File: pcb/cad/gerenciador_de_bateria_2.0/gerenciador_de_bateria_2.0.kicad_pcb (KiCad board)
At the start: 2 copper layers, 37 parts, among them J1 Conn_01x01_Female, J10 Conn_01x01_Female, J2 Conn_01x01_Female, J3 Conn_01x01_Female, J4 Conn_01x01_Female, J5 Conn_01x02_Male, J6 Conn_01x01_Female, J7 Conn_01x01_Female, J8 Conn_01x01_Female, J9 Conn_01x01_Female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

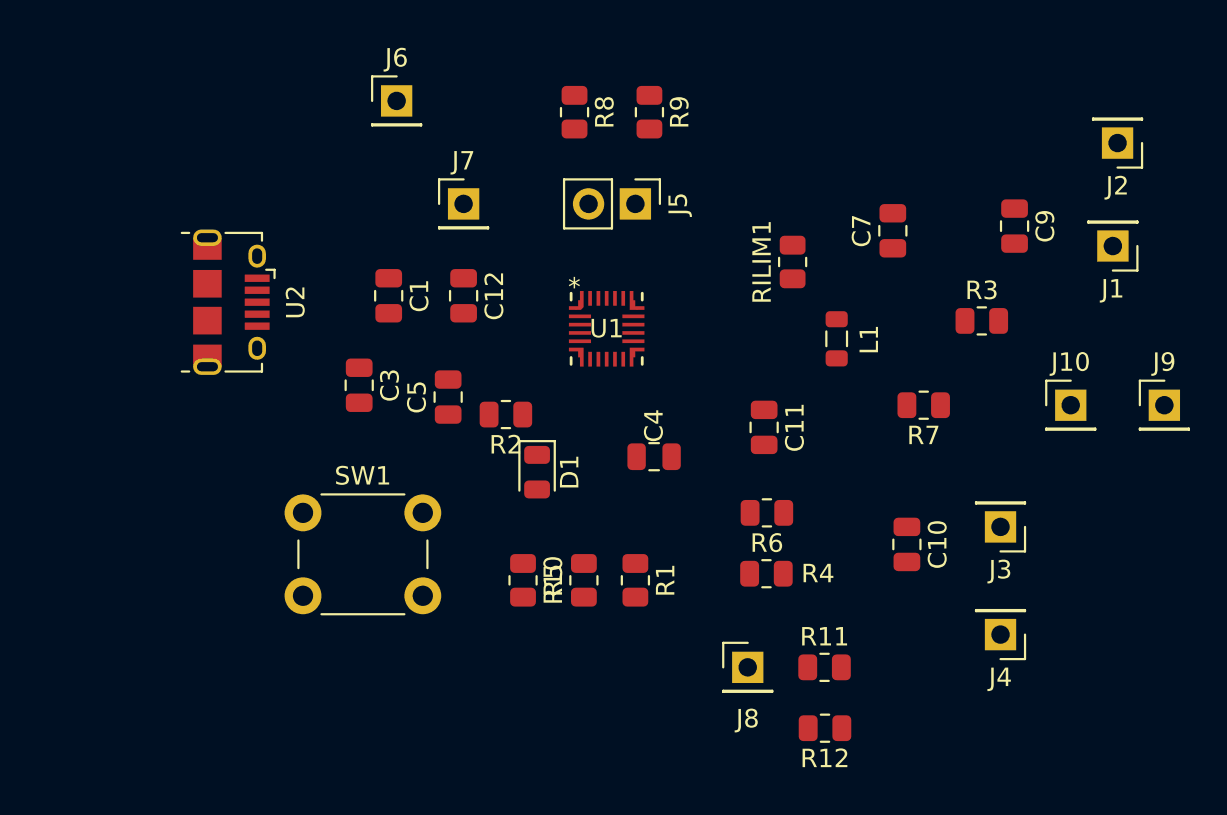
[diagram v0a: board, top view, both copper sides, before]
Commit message: Alteração no GND do esquemático para GNDA ou GNDPWR, finalização da PCB do gerenciador de bateria 2.0
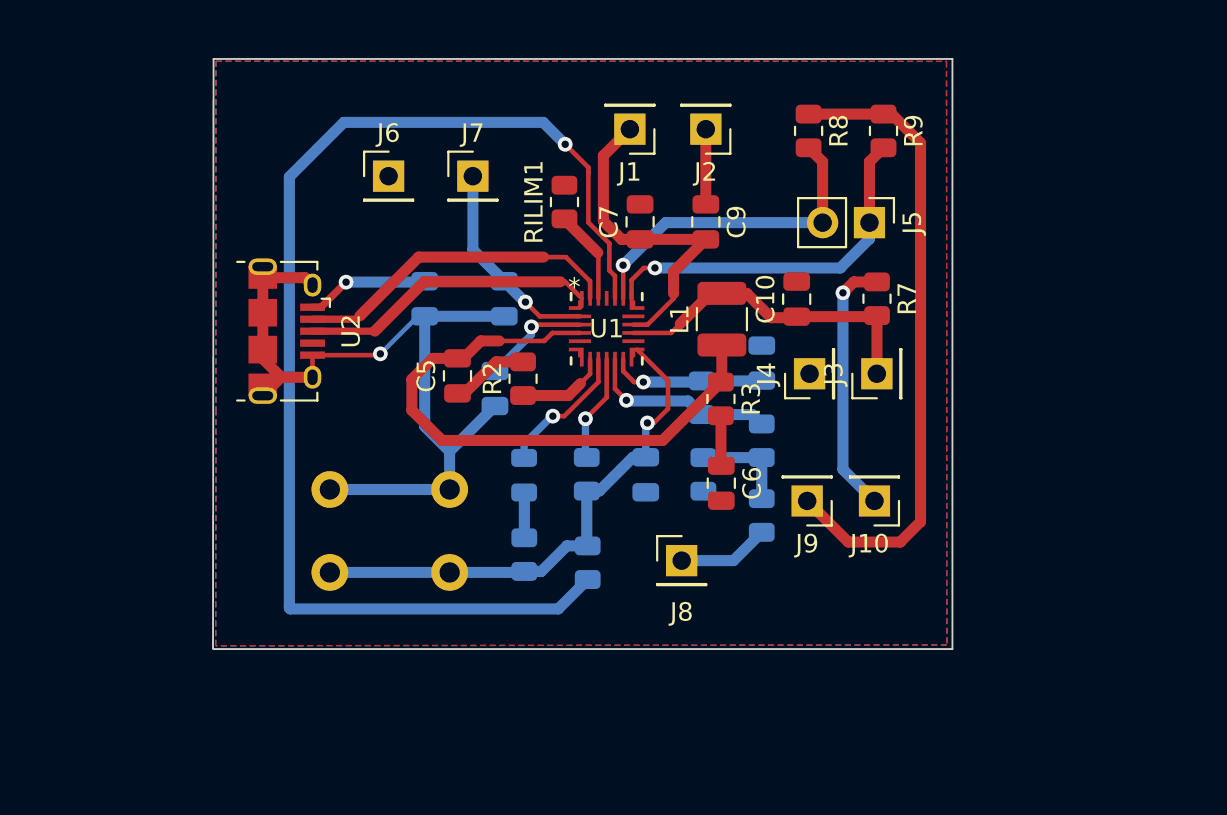
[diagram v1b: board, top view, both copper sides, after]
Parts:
- added C6: NC, Capacitor_SMD:C_0805_2012Metric, F.Cu at (125.8, 131.0)
- C1, C11, C12, C3, C4, D1, R1, R10, R11, R12, R4, R5, R6, SW1: moved to B.Cu
- L1: footprint Inductor_SMD:L_0805_2012Metric -> Inductor_SMD:L_1210_3225Metric
- moved J1 27.0 mm to (120.9, 111.8)
- moved J2 22.4 mm to (125.0, 111.8)
- moved J9 20.1 mm to (130.5, 131.9), turned to 180 degrees
- moved J4 17.5 mm to (130.6, 125.0), turned to 90 degrees
- moved C9 16.8 mm to (125.0, 116.8)
- moved R12 15.3 mm to (124.8, 130.5), turned to -90 degrees
- moved R3 14.8 mm to (125.8, 126.4), turned to -90 degrees
- moved C10 14.6 mm to (129.9, 121.0), turned to 90 degrees
- moved C7 13.7 mm to (121.4, 116.8)
- moved RILIM1 12.8 mm to (117.3, 115.7)
- moved R8 12.7 mm to (130.6, 111.9)
- moved J5 12.7 mm to (133.9, 116.8)
- moved R9 12.7 mm to (134.6, 111.9)
- moved J10 11.8 mm to (134.1, 131.9), turned to 180 degrees
- moved J3 10.7 mm to (134.3, 125.0), turned to 90 degrees
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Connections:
- C1 pad 2: GND -> GNDA
- C10 pad 2: GNDPWR -> GNDA
- C11 pad 1: GND -> GNDA
- C12 pad 2: GND -> GNDA
- C3 pad 2: GNDPWR -> GNDA
- C7 pad 2: GND -> GNDA
- C9 pad 1: GNDPWR -> GNDA
- J2 pad 1: GNDPWR -> GNDA
- J4 pad 1: GNDPWR -> GNDA
- J6 pad 1: GND -> GNDA
- RILIM1 pad 2: GND -> GNDA
- U1 pad 14: (no net) -> /VREF
- U1 pad 15: GND -> GNDA
- U1 pad 5: GND -> GNDA
- U1 pad 7: GND -> GNDA
- U2 pad 5: GND -> GNDA
- U2 pad 6: GND -> GNDA
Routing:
- net Net-(R1-Pad1): track 0.00 -> 66.4 mm, vias 0 -> 1
- net GNDA: track 0.00 -> 48.9 mm, vias 0 -> 1
- net /VDD: track 0.00 -> 34.8 mm
- net Net-(C5-Pad2): track 0.00 -> 32.6 mm
- net /VREF: track 0.00 -> 29.1 mm, vias 0 -> 1
- net Net-(C1-Pad1): track 0.00 -> 22.3 mm, vias 0 -> 2
- net /SCL: track 0.00 -> 20.1 mm, vias 0 -> 1
- net Net-(C7-Pad1): track 0.00 -> 18.7 mm
- net /SYS: track 0.00 -> 18.2 mm
- net /SDA: track 0.00 -> 18.0 mm, vias 0 -> 1
- net Net-(U2-Pad2): track 0.00 -> 17.9 mm
- net Net-(U2-Pad3): track 0.00 -> 16.1 mm
- net Net-(J10-Pad1): track 0.00 -> 14.1 mm, vias 0 -> 1
- net Net-(R4-Pad1): track 0.00 -> 10.4 mm, vias 0 -> 1
- net Net-(C11-Pad2): track 0.00 -> 8.44 mm, vias 0 -> 1
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- added copper zone on B.Cu, net GNDA
- added copper zone on F.Cu, net GNDA
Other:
- board outline added: 40.1 x 32 mm

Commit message: Otimização do esquemático do gerenciador_de_bateria, PCB atualizada com o USB centralizado no gerenciador_de_bateria_2.0, no gerenciador_de_bateria a PCB foi inicializada e finalizada
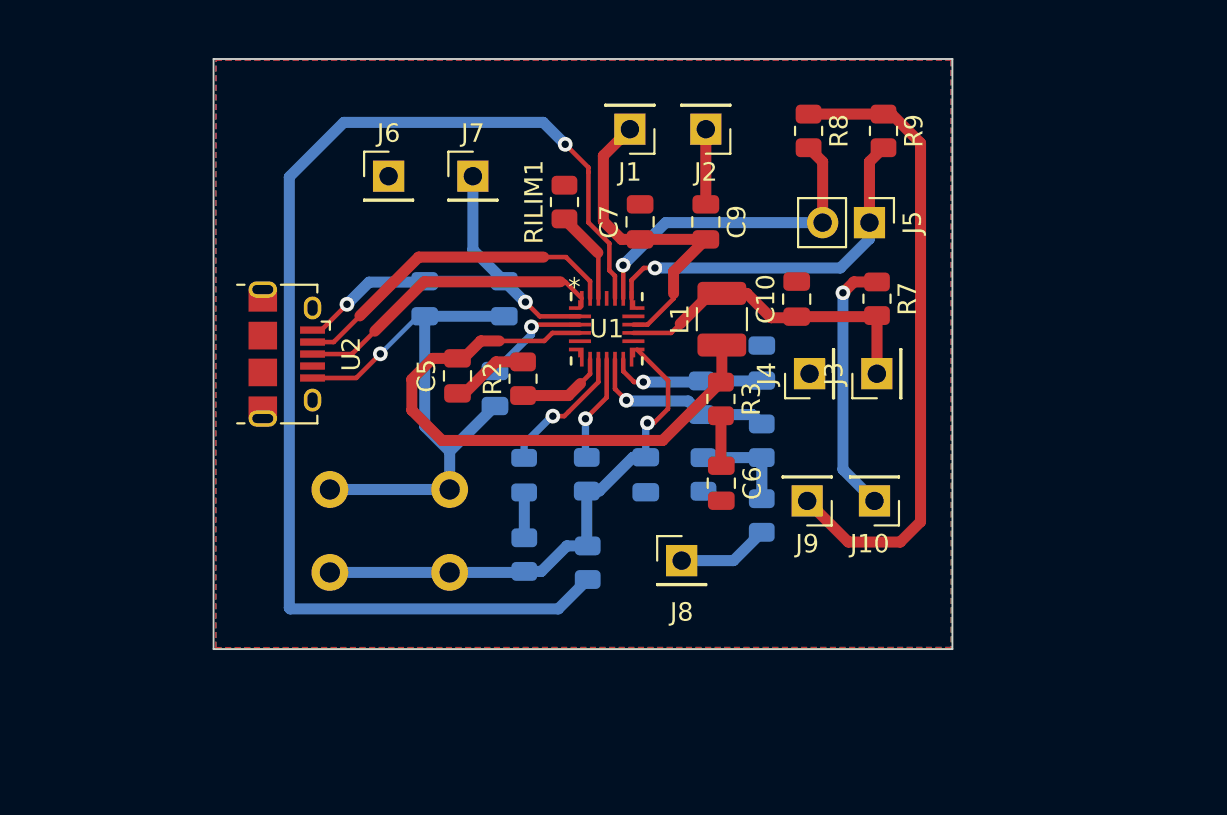
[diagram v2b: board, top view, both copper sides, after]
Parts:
- moved U2 1.24 mm to (102.2, 124.0)
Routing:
- net GNDA: track 48.9 -> 35.8 mm
- net Net-(C1-Pad1): track 22.3 -> 22.8 mm
- net Net-(U2-Pad3): track 16.1 -> 16.6 mm
- net Net-(U2-Pad2): track 17.9 -> 18.4 mm
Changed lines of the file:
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@@
   )
   (footprint "Connector_USB:USB_Micro-B_Amphenol_10118194_Horizontal" (layer "F.Cu")
-    (at 102.24 122.73 -90)
+    (at 102.24 123.97 -90)
     (descr "USB Micro-B receptacle, horizontal, SMD, 10118194, https://cdn.amphenol-icc.com/media/wysiwyg/files/drawing/10118194.pdf")
     (tags "USB Micro B horizontal SMD")
@@
     )
   )
-  (gr_line (start 98.25 139.98) (end 138.36 139.98) (layer "Edge.Cuts") (width 0.1))
+  (gr_line (start 98.27 139.98) (end 138.36 139.98) (layer "Edge.Cuts") (width 0.1))
   (gr_line (start 138.36 139.98) (end 138.36 107.96) (layer "Edge.Cuts") (width 0.1))
-  (gr_line (start 98.27 107.96) (end 98.24 139.93) (layer "Edge.Cuts") (width 0.1))
+  (gr_line (start 98.27 107.96) (end 98.27 139.98) (layer "Edge.Cuts") (width 0.1))
   (gr_line (start 138.36 107.96) (end 98.27 107.96) (layer "Edge.Cuts") (width 0.1))
-  (segment (start 104.1 121.43) (end 103.64 121.43) (width 0.4) (layer "F.Cu") (net 1))
   (segment (start 115.967735 121.925) (end 115.192816 121.150081) (width 0.25) (layer "F.Cu") (net 1))
-  (segment (start 105.46 120.07) (end 104.1 121.43) (width 0.4) (layer "F.Cu") (net 1))
+  (segment (start 103.64 122.67) (end 104.115 122.67) (width 0.25) (layer "F.Cu") (net 1))
+  (segment (start 104.115 122.67) (end 105.46 121.325) (width 0.25) (layer "F.Cu") (net 1))
+  (segment (start 105.46 121.325) (end 105.46 121.32) (width 0.25) (layer "F.Cu") (net 1))
+  (segment (start 105.46 121.32) (end 105.51 121.27) (width 0.25) (layer "F.Cu") (net 1))
   (segment (start 118.15 121.925) (end 115.967735 121.925) (width 0.25) (layer "F.Cu") (net 1))
   (via (at 115.192816 121.150081) (size 0.8) (drill 0.4) (layers "F.Cu" "B.Cu") (net 1))
-  (via (at 105.46 120.07) (size 0.8) (drill 0.4) (layers "F.Cu" "B.Cu") (net 1))
+  (via (at 105.51 121.27) (size 0.8) (drill 0.4) (layers "F.Cu" "B.Cu") (net 1))
   (segment (start 112.34 118.314) (end 114.046 120.02) (width 0.6) (layer "B.Cu") (net 1))
   (segment (start 114.046 120.026) (end 115.18 121.16) (width 0.6) (layer "B.Cu") (net 1))
+  (segment (start 106.71 120.07) (end 109.678 120.07) (width 0.6) (layer "B.Cu") (net 1))
   (segment (start 112.34 114.32) (end 112.34 118.314) (width 0.6) (layer "B.Cu") (net 1))
   (segment (start 109.728 120.02) (end 114.046 120.02) (width 0.6) (layer "B.Cu") (net 1))
+  (segment (start 114.046 120.02) (end 114.046 120.026) (width 0.6) (layer "B.Cu") (net 1))
   (segment (start 109.678 120.07) (end 109.728 120.02) (width 0.6) (layer "B.Cu") (net 1))
-  (segment (start 114.046 120.02) (end 114.046 120.026) (width 0.6) (layer "B.Cu") (net 1))
-  (segment (start 105.46 120.07) (end 109.678 120.07) (width 0.6) (layer "B.Cu") (net 1))
+  (segment (start 105.51 121.27) (end 106.71 120.07) (width 0.6) (layer "B.Cu") (net 1))
   (segment (start 115.636603 122.374999) (end 115.518328 122.493274) (width 0.25) (layer "F.Cu") (net 2))
   (segment (start 118.15 122.374999) (end 115.636603 122.374999) (width 0.25) (layer "F.Cu") (net 2))
@@
   (segment (start 110.907 136.235) (end 110.744 136.072) (width 0.6) (layer "B.Cu") (net 3))
   (segment (start 115.075 135.82) (end 115.13 135.765) (width 0.6) (layer "B.Cu") (net 3))
-  (segment (start 107.25 124.03) (end 107.32 123.96) (width 0.25) (layer "F.Cu") (net 4))
-  (segment (start 103.64 125.23) (end 101.94 125.23) (width 0.6) (layer "F.Cu") (net 4))
-  (segment (start 100.94 123.73) (end 100.94 121.73) (width 0.6) (layer "F.Cu") (net 4))
   (segment (start 124.98 115.85) (end 124.98 111.77) (width 0.6) (layer "F.Cu") (net 4))
-  (segment (start 100.94 119.83) (end 103.24 119.83) (width 0.6) (layer "F.Cu") (net 4))
-  (segment (start 100.94 123.73) (end 100.94 124.23) (width 0.6) (layer "F.Cu") (net 4))
-  (segment (start 100.94 121.73) (end 100.94 119.83) (width 0.6) (layer "F.Cu") (net 4))
-  (segment (start 101.94 125.23) (end 100.94 126.23) (width 0.6) (layer "F.Cu") (net 4))
-  (segment (start 103.64 124.03) (end 107.25 124.03) (width 0.25) (layer "F.Cu") (net 4))
-  (segment (start 100.94 124.23) (end 101.94 125.23) (width 0.6) (layer "F.Cu") (net 4))
-  (segment (start 100.94 119.23) (end 100.94 119.83) (width 0.6) (layer "F.Cu") (net 4))
-  (segment (start 103.64 124.03) (end 103.64 125.23) (width 0.25) (layer "F.Cu") (net 4))
-  (segment (start 103.24 119.83) (end 103.64 120.23) (width 0.6) (layer "F.Cu") (net 4))
+  (segment (start 106.01 125.27) (end 107.32 123.96) (width 0.25) (layer "F.Cu") (net 4))
+  (segment (start 103.64 125.27) (end 106.01 125.27) (width 0.25) (layer "F.Cu") (net 4))
   (via (at 107.32 123.96) (size 0.8) (drill 0.4) (layers "F.Cu" "B.Cu") (net 4))
   (segment (start 109.728 127.898) (end 111.08 129.25) (width 0.6) (layer "B.Cu") (net 4))
@@
   (segment (start 118.699999 120.019999) (end 118.699999 120.950001) (width 0.25) (layer "F.Cu") (net 25))
   (segment (start 109.4 118.71) (end 106.21 121.9) (width 0.6) (layer "F.Cu") (net 25))
+  (segment (start 104.79 123.32) (end 106.21 121.9) (width 0.25) (layer "F.Cu") (net 25))
   (segment (start 116.18 118.71) (end 117.39 118.71) (width 0.25) (layer "F.Cu") (net 25))
-  (segment (start 106.03 122.08) (end 103.64 122.08) (width 0.4) (layer "F.Cu") (net 25))
-  (segment (start 106.21 121.9) (end 106.03 122.08) (width 0.4) (layer "F.Cu") (net 25))
   (segment (start 116.18 118.71) (end 109.4 118.71) (width 0.6) (layer "F.Cu") (net 25))
   (segment (start 117.39 118.71) (end 118.699999 120.019999) (width 0.25) (layer "F.Cu") (net 25))
+  (segment (start 103.64 123.32) (end 104.79 123.32) (width 0.25) (layer "F.Cu") (net 25))
   (segment (start 117.09 120.05) (end 109.7 120.05) (width 0.6) (layer "F.Cu") (net 26))
+  (segment (start 103.64 123.97) (end 105.78 123.97) (width 0.25) (layer "F.Cu") (net 26))
   (segment (start 118.25 120.950001) (end 117.349999 120.05) (width 0.25) (layer "F.Cu") (net 26))
-  (segment (start 107.02 122.73) (end 103.64 122.73) (width 0.4) (layer "F.Cu") (net 26))
   (segment (start 109.7 120.05) (end 107.02 122.73) (width 0.6) (layer "F.Cu") (net 26))
   (segment (start 117.349999 120.05) (end 117.09 120.05) (width 0.25) (layer "F.Cu") (net 26))
+  (segment (start 105.78 123.97) (end 107.02 122.73) (width 0.25) (layer "F.Cu") (net 26))
   (zone (net 4) (net_name "GNDA") (layers F&B.Cu) (hatch edge 0.508)
     (connect_pads (clearance 0.508))
@@
     (polygon
       (pts
-        (xy 138.04 108.09)
-        (xy 138.06 139.75)
-        (xy 98.39 139.8)
-        (xy 98.4 127.13)
-        (xy 98.4 108.08)
+        (xy 138.29 139.89)
+        (xy 98.39 139.9)
+        (xy 98.4 108.05)
+        (xy 98.4 108.03)
+        (xy 138.28 108.03)
       )
     )

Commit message: Alterações no lauout de PCB
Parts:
- removed J10, J9: Conn_01x01_Female, Connector_PinHeader_2.54mm:PinHeader_1x01_P2.54mm_Vertical
- removed R9: 10k, Resistor_SMD:R_0805_2012Metric
- R7: value 0 -> 10k; moved to B.Cu
- R8: moved to B.Cu
- moved J1 14.0 mm to (133.3, 118.1), turned to 0 degrees
- moved J2 12.7 mm to (133.3, 121.3), turned to 90 degrees
- moved R8 8.79 mm to (130.8, 120.7), turned to 90 degrees
- moved C6 5.93 mm to (129.5, 126.4), turned to 90 degrees
- moved C7 4.51 mm to (125.7, 118.1), turned to 0 degrees
- moved J5 4.50 mm to (129.5, 115.6)
- moved C5 4.18 mm to (114.3, 128.3), turned to -90 degrees
- moved C9 3.92 mm to (125.7, 120.7), turned to 180 degrees
- moved J4 2.80 mm to (133.3, 124.5), turned to 0 degrees
- moved J3 2.60 mm to (133.3, 127.5), turned to 0 degrees
- moved R3 2.50 mm to (125.7, 128.9), turned to 0 degrees
- moved L1 2.38 mm to (125.7, 124.5)
- moved C10 1.00 mm to (129.5, 121.9)
- moved R7 0.43 mm to (134.0, 120.7), turned to 90 degrees
- moved R2 0.21 mm to (115.1, 125.1), turned to 180 degrees
- renumbered J8 to TERM1
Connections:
- C1 pad 2: GNDA -> GNDPWR
- C10 pad 2: GNDA -> GNDPWR
- C12 pad 1: Net-(C1-Pad1) -> Net-(C12-Pad1)
- C12 pad 2: GNDA -> GNDPWR
- C3 pad 2: GNDA -> GNDPWR
- C6 pad 2: GNDA -> GNDPWR
- C7 pad 2: GNDA -> GNDPWR
- C9 pad 1: GNDA -> GNDPWR
- J2 pad 1: GNDA -> GNDPWR
- J4 pad 1: GNDA -> GNDPWR
- J6 pad 1: GNDA -> GNDPWR
- J7 pad 1: Net-(C1-Pad1) -> Net-(C12-Pad1)
- R7 pad 1: Net-(J10-Pad1) -> /SYS
- R7 pad 2: /SYS -> /SCL
- R8 pad 1: /VDD -> /SYS
- U1 pad 2: Net-(C1-Pad1) -> Net-(C12-Pad1)
- U1 pad 5: GNDA -> GNDPWR
- U1 pad 7: GNDA -> GNDPWR
- U2 pad 1: Net-(C1-Pad1) -> Net-(C12-Pad1)
- U2 pad 5: GNDA -> GNDPWR
- U2 pad 6: GNDA -> GNDPWR
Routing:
- net GNDA: track 35.8 -> 0.00 mm, vias 1 -> 0
- net /VDD: track 34.8 -> 0.00 mm
- net GNDPWR: track 0.00 -> 31.7 mm, vias 0 -> 1
- net Net-(C5-Pad2): track 32.6 -> 5.88 mm
- net Net-(C12-Pad1): track 0.00 -> 22.8 mm, vias 0 -> 2
- net Net-(C1-Pad1): track 22.8 -> 0.00 mm, vias 2 -> 0
- net /SYS: track 18.2 -> 0.01 mm
- net /SCL: track 20.1 -> 2.53 mm, vias 1 -> 0
- net /SDA: track 18.0 -> 1.80 mm, vias 1 -> 0
- net Net-(C7-Pad1): track 18.7 -> 3.04 mm
- net Net-(J10-Pad1): track 14.1 -> 0.00 mm, vias 1 -> 0
- net Net-(C5-Pad1): track 4.79 -> 0.00 mm
- net Net-(C6-Pad1): track 2.72 -> 0.00 mm
- net Net-(R2-Pad1): track 4.92 -> 2.46 mm
